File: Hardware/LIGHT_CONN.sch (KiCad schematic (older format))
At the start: 72 parts

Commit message: Added PWM generator, More Shift Regs
Moved GPIO pins on MUSE
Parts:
- added R? (x6): 4.7K, symbol R
- added U?: PCA9685BS, symbol PCA9685BS
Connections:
- net labels added: +3.3V, PWM_SCL, PWM_SDA, ~PWM_OE
- wire segments 168 -> 205
- no-connect marks 0 -> 4
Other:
- note added: "RGB LED Strip PWM Generator"
- moved on the sheet: P?, Q?, R?

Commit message: Syncing changes from 9/20 meeting
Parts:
- removed R? (x6): 4.7K, symbol R
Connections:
- net labels removed: ~PWM_OE
- wire segments 205 -> 183

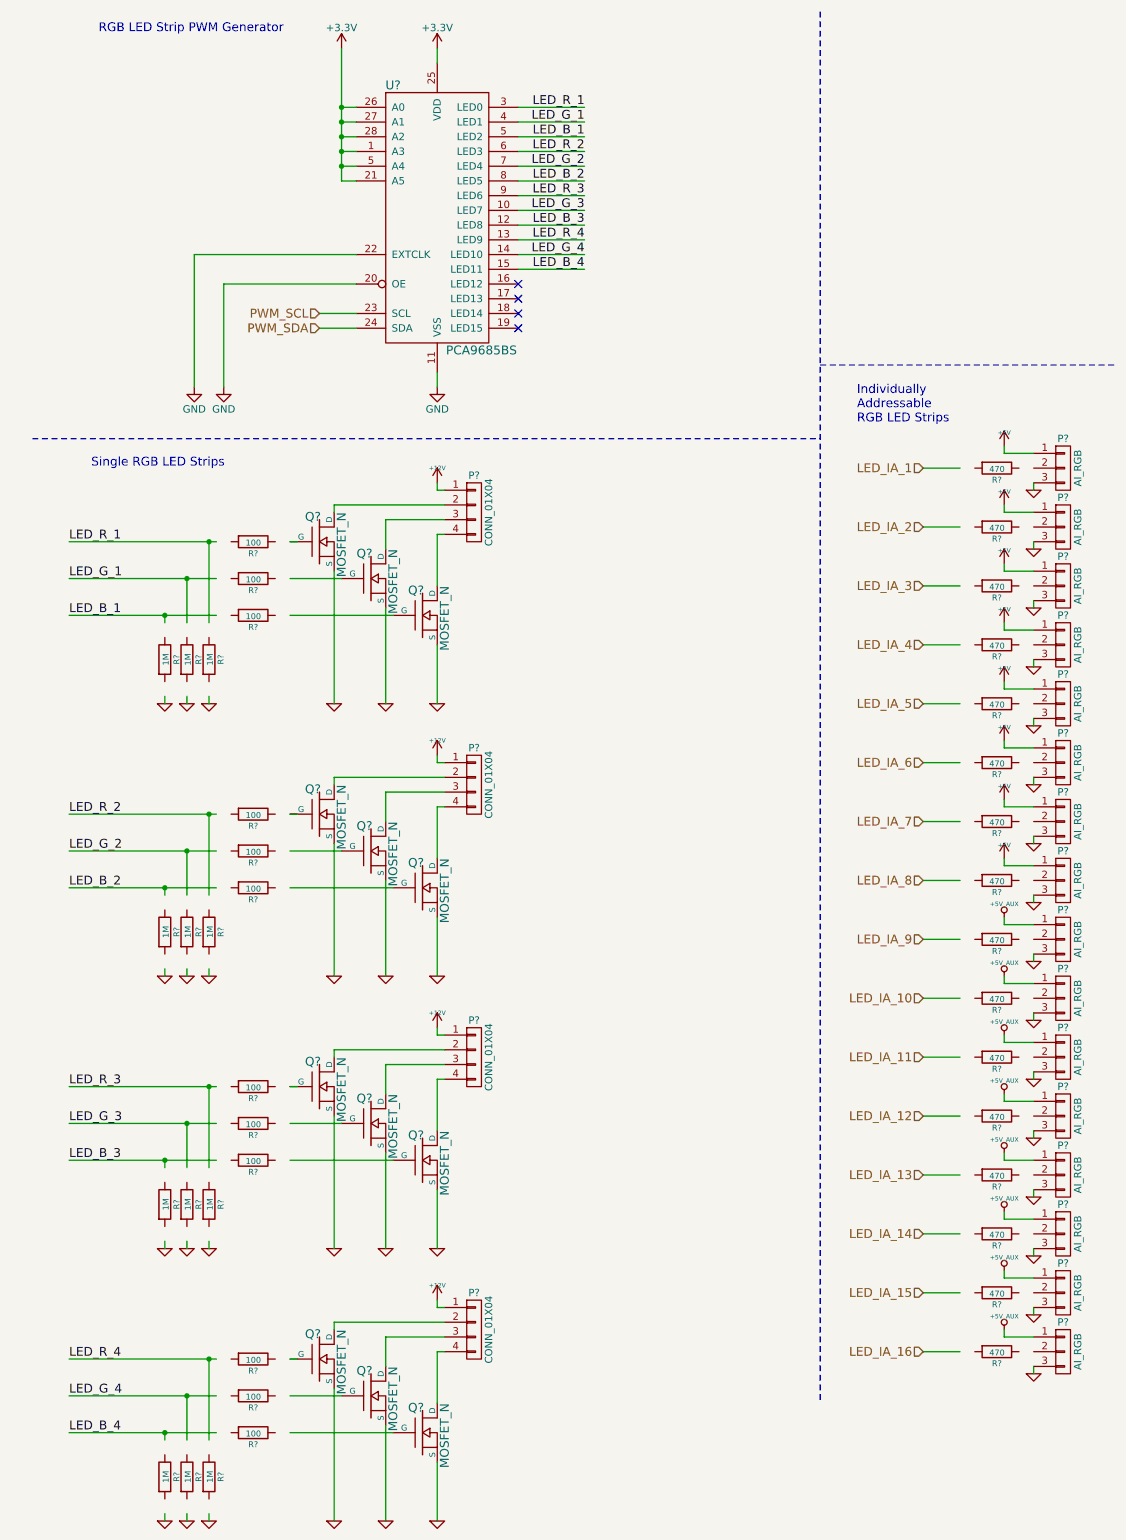
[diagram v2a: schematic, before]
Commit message: Currently adding level shifters
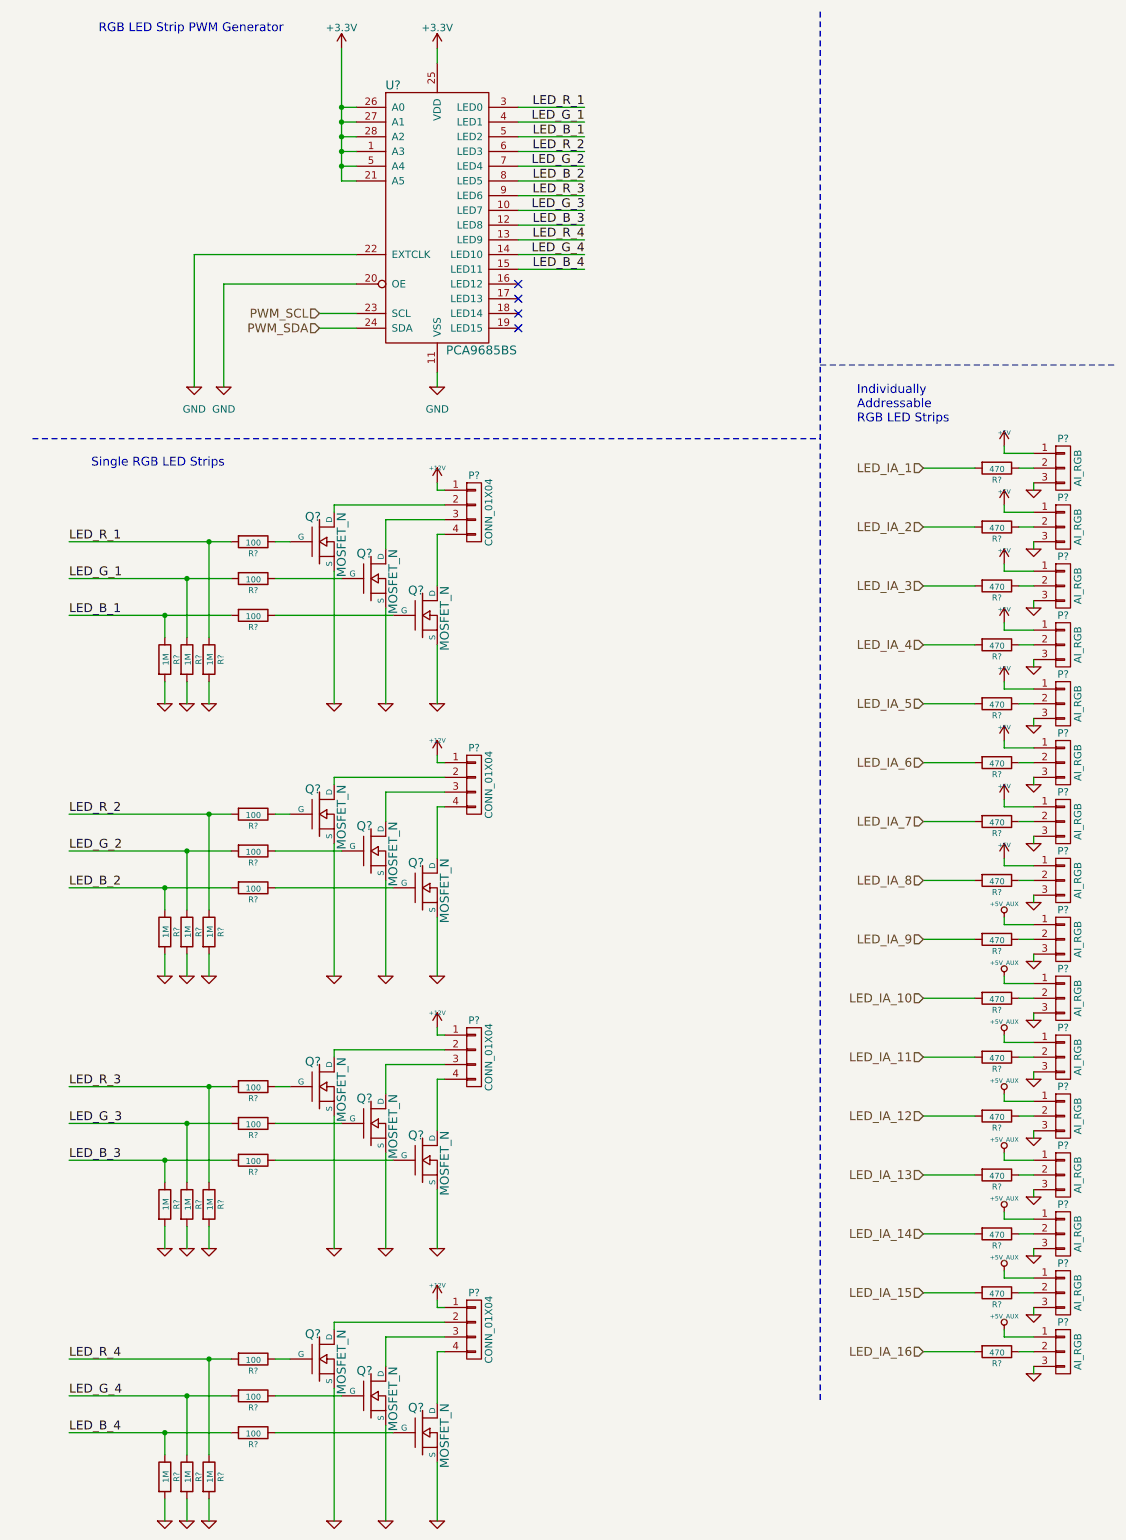
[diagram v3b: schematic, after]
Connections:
- wire segments 183 -> 199
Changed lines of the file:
@@
 LIBS:microchip_pic18mcu
 LIBS:microchip
+LIBS:microchip1
 LIBS:microcontrollers
 LIBS:motorola
@@
 LIBS:sensors
 LIBS:siliconi
+LIBS:special
 LIBS:stm8
 LIBS:stm32
@@
 F 3 "" H 3200 5550 60  0000 C CNN
 	1    3200 5550
-	1    0    0    -1
-$EndComp
-$Comp
-L MOSFET_N Q?
-U 1 1 57E232B5
-P 2400 5950
-F 0 "Q?" H 2410 6120 60  0000 R CNN
-F 1 "MOSFET_N" V 2550 6150 60  0000 R CNN
-F 2 "" H 2400 5950 60  0000 C CNN
-F 3 "" H 2400 5950 60  0000 C CNN
-	1    2400 5950
 	1    0    0    -1
 $EndComp
@@
 $EndComp
 $Comp
-L GND #PWR?
+L GND-RESCUE-museV2 #PWR?
 U 1 1 57E62373
 P 3200 3050
@@
 $EndComp
 $Comp
-L +3.3V #PWR?
+L +3.3V-RESCUE-museV2 #PWR?
 U 1 1 57E6273F
 P 3200 750
+AR Path="/57E6273F" Ref="#PWR?"  Part="1"
+AR Path="/57E226F1/57E6273F" Ref="#PWR?"  Part="1"
 F 0 "#PWR?" H 3200 600 50  0001 C CNN
 F 1 "+3.3V" H 3200 890 50  0000 C CNN
@@
 PWM_SDA
 $Comp
-L GND #PWR?
+L GND-RESCUE-museV2 #PWR?
 U 1 1 57E689F1
 P 1550 3050
@@
 	7250 9750 7250 9700
 Wire Wire Line
-	6500 3600 6750 3600
-Wire Wire Line
-	6750 4000 6500 4000
-Wire Wire Line
-	6750 4400 6500 4400
-Wire Wire Line
-	6750 4800 6500 4800
-Wire Wire Line
-	6750 5200 6500 5200
-Wire Wire Line
-	6750 5600 6500 5600
-Wire Wire Line
-	6750 6000 6500 6000
-Wire Wire Line
-	6500 6400 6750 6400
-Wire Wire Line
-	6750 6800 6500 6800
-Wire Wire Line
-	6500 7200 6750 7200
-Wire Wire Line
-	6750 7600 6500 7600
-Wire Wire Line
-	6500 8000 6750 8000
-Wire Wire Line
-	6750 8400 6500 8400
-Wire Wire Line
-	6500 8800 6750 8800
-Wire Wire Line
-	6750 9200 6500 9200
-Wire Wire Line
-	6500 9600 6750 9600
-Wire Wire Line
-	700  4600 1700 4600
-Wire Wire Line
-	700  4350 1700 4350
-Wire Wire Line
-	700  4100 1700 4100
-Wire Wire Line
-	2200 4100 2250 4100
-Wire Wire Line
-	2200 4350 2550 4350
-Wire Wire Line
-	2200 4600 2900 4600
+	6500 3600 6850 3600
+Wire Wire Line
+	6500 4000 6850 4000
+Wire Wire Line
+	6500 4400 6850 4400
+Wire Wire Line
+	6500 4800 6850 4800
+Wire Wire Line
+	6500 5200 6850 5200
+Wire Wire Line
+	6500 5600 6850 5600
+Wire Wire Line
+	6500 6000 6850 6000
+Wire Wire Line
+	6500 6400 6850 6400
+Wire Wire Line
+	6500 6800 6850 6800
+Wire Wire Line
+	6500 7200 6850 7200
+Wire Wire Line
+	6500 7600 6850 7600
+Wire Wire Line
+	6500 8000 6850 8000
+Wire Wire Line
+	6500 8400 6850 8400
+Wire Wire Line
+	6500 8800 6850 8800
+Wire Wire Line
+	6500 9200 6850 9200
+Wire Wire Line
+	6500 9600 6850 9600
+Wire Wire Line
+	700  4600 1800 4600
+Wire Wire Line
+	700  4350 1800 4350
+Wire Wire Line
+	700  4100 1800 4100
+Wire Wire Line
+	2100 4350 2550 4350
+Wire Wire Line
+	2100 4600 2900 4600
 Wire Wire Line
 	2850 4550 2850 5200
@@
 	2500 4300 2500 5200
 Wire Wire Line
-	1350 4650 1350 4600
+	1350 4600 1350 4750
 Connection ~ 1350 4600
 Wire Wire Line
-	1500 4650 1500 4350
+	1500 4350 1500 4750
 Connection ~ 1500 4350
 Wire Wire Line
-	1650 4650 1650 4100
+	1650 4100 1650 4750
 Connection ~ 1650 4100
 Wire Wire Line
-	1350 5200 1350 5150
-Wire Wire Line
-	1500 5200 1500 5150
-Wire Wire Line
-	1650 5200 1650 5150
+	1350 5050 1350 5200
+Wire Wire Line
+	1500 5050 1500 5200
+Wire Wire Line
+	1650 5050 1650 5200
 Wire Wire Line
 	3200 5550 3200 5600
@@
 	3200 7050 3200 6650
 Wire Wire Line
-	700  6450 1700 6450
-Wire Wire Line
-	700  6200 1700 6200
-Wire Wire Line
-	700  5950 1700 5950
-Wire Wire Line
-	2200 5950 2250 5950
-Wire Wire Line
-	2200 6200 2550 6200
-Wire Wire Line
-	2200 6450 2900 6450
+	700  6450 1800 6450
+Wire Wire Line
+	700  6200 1800 6200
+Wire Wire Line
+	700  5950 1800 5950
+Wire Wire Line
+	2100 6200 2550 6200
+Wire Wire Line
+	2100 6450 2900 6450
 Wire Wire Line
 	2850 6400 2850 7050
@@
 	2500 6150 2500 7050
 Wire Wire Line
-	1350 6500 1350 6450
+	1350 6450 1350 6600
 Connection ~ 1350 6450
 Wire Wire Line
-	1500 6500 1500 6200
+	1500 6200 1500 6600
 Connection ~ 1500 6200
 Wire Wire Line
-	1650 6500 1650 5950
+	1650 5950 1650 6600
 Connection ~ 1650 5950
 Wire Wire Line
-	1350 7050 1350 7000
-Wire Wire Line
-	1500 7050 1500 7000
-Wire Wire Line
-	1650 7050 1650 7000
+	1350 6900 1350 7050
+Wire Wire Line
+	1500 6900 1500 7050
+Wire Wire Line
+	1650 6900 1650 7050
 Wire Wire Line
 	3200 7400 3200 7450
@@
 	3200 8900 3200 8500
 Wire Wire Line
-	700  8300 1700 8300
-Wire Wire Line
-	700  8050 1700 8050
-Wire Wire Line
-	700  7800 1700 7800
-Wire Wire Line
-	2200 7800 2250 7800
-Wire Wire Line
-	2200 8050 2550 8050
-Wire Wire Line
-	2200 8300 2900 8300
+	700  8300 1800 8300
+Wire Wire Line
+	700  8050 1800 8050
+Wire Wire Line
+	700  7800 1800 7800
+Wire Wire Line
+	2100 8050 2550 8050
+Wire Wire Line
+	2100 8300 2900 8300
 Wire Wire Line
 	2850 8250 2850 8900
@@
 	2500 8000 2500 8900
 Wire Wire Line
-	1350 8350 1350 8300
+	1350 8300 1350 8450
 Connection ~ 1350 8300
 Wire Wire Line
-	1500 8350 1500 8050
+	1500 8050 1500 8450
 Connection ~ 1500 8050
 Wire Wire Line
-	1650 8350 1650 7800
+	1650 7800 1650 8450
 Connection ~ 1650 7800
 Wire Wire Line
-	1350 8900 1350 8850
-Wire Wire Line
-	1500 8900 1500 8850
-Wire Wire Line
-	1650 8900 1650 8850
+	1350 8750 1350 8900
+Wire Wire Line
+	1500 8750 1500 8900
+Wire Wire Line
+	1650 8750 1650 8900
 Wire Wire Line
 	3200 9250 3200 9300
@@
 	3200 10750 3200 10350
 Wire Wire Line
-	700  10150 1700 10150
-Wire Wire Line
-	700  9900 1700 9900
-Wire Wire Line
-	700  9650 1700 9650
-Wire Wire Line
-	2200 9650 2250 9650
-Wire Wire Line
-	2200 9900 2550 9900
-Wire Wire Line
-	2200 10150 2900 10150
+	700  10150 1800 10150
+Wire Wire Line
+	700  9900 1800 9900
+Wire Wire Line
+	700  9650 1800 9650
+Wire Wire Line
+	2100 9900 2550 9900
+Wire Wire Line
+	2100 10150 2900 10150
 Wire Wire Line
 	2850 10100 2850 10750
@@
 	2500 9850 2500 10750
 Wire Wire Line
-	1350 10200 1350 10150
+	1350 10150 1350 10300
 Connection ~ 1350 10150
 Wire Wire Line
-	1500 10200 1500 9900
+	1500 9900 1500 10300
 Connection ~ 1500 9900
 Wire Wire Line
-	1650 10200 1650 9650
+	1650 9650 1650 10300
 Connection ~ 1650 9650
 Wire Wire Line
-	1350 10750 1350 10700
-Wire Wire Line
-	1500 10750 1500 10700
-Wire Wire Line
-	1650 10750 1650 10700
+	1350 10600 1350 10750
+Wire Wire Line
+	1500 10600 1500 10750
+Wire Wire Line
+	1650 10600 1650 10750
 Text Notes 900  650  0    60   ~ 0
 RGB LED Strip PWM Generator
 $Comp
-L +3.3V #PWR?
+L +3.3V-RESCUE-museV2 #PWR?
 U 1 1 57EA76FD
 P 2550 750
+AR Path="/57EA76FD" Ref="#PWR?"  Part="1"
+AR Path="/57E226F1/57EA76FD" Ref="#PWR?"  Part="1"
 F 0 "#PWR?" H 2550 600 50  0001 C CNN
 F 1 "+3.3V" H 2550 890 50  0000 C CNN
@@
 Connection ~ 2550 1150
 $Comp
-L GND #PWR?
+L GND-RESCUE-museV2 #PWR?
 U 1 1 57EF1660
 P 1750 3050
@@
 Wire Wire Line
 	1750 2350 2650 2350
+Wire Wire Line
+	2200 9650 2100 9650
+Wire Wire Line
+	2200 7800 2100 7800
+$Comp
+L MOSFET_N Q?
+U 1 1 57E232B5
+P 2400 5950
+F 0 "Q?" H 2410 6120 60  0000 R CNN
+F 1 "MOSFET_N" V 2550 6150 60  0000 R CNN
+F 2 "" H 2400 5950 60  0000 C CNN
+F 3 "" H 2400 5950 60  0000 C CNN
+	1    2400 5950
+	1    0    0    -1
+$EndComp
+Wire Wire Line
+	2200 5950 2100 5950
+Wire Wire Line
+	2200 4100 2100 4100
+Wire Wire Line
+	7150 3600 7250 3600
+Wire Wire Line
+	7150 4000 7250 4000
+Wire Wire Line
+	7250 4400 7150 4400
+Wire Wire Line
+	7150 4800 7250 4800
+Wire Wire Line
+	7250 5200 7150 5200
+Wire Wire Line
+	7150 5600 7250 5600
+Wire Wire Line
+	7250 6000 7150 6000
+Wire Wire Line
+	7150 6400 7250 6400
+Wire Wire Line
+	7250 6800 7150 6800
+Wire Wire Line
+	7150 7200 7250 7200
+Wire Wire Line
+	7250 7600 7150 7600
+Wire Wire Line
+	7150 8000 7250 8000
+Wire Wire Line
+	7250 8400 7150 8400
+Wire Wire Line
+	7250 8800 7150 8800
+Wire Wire Line
+	7150 9200 7250 9200
+Wire Wire Line
+	7250 9600 7150 9600
 $EndSCHEMATC

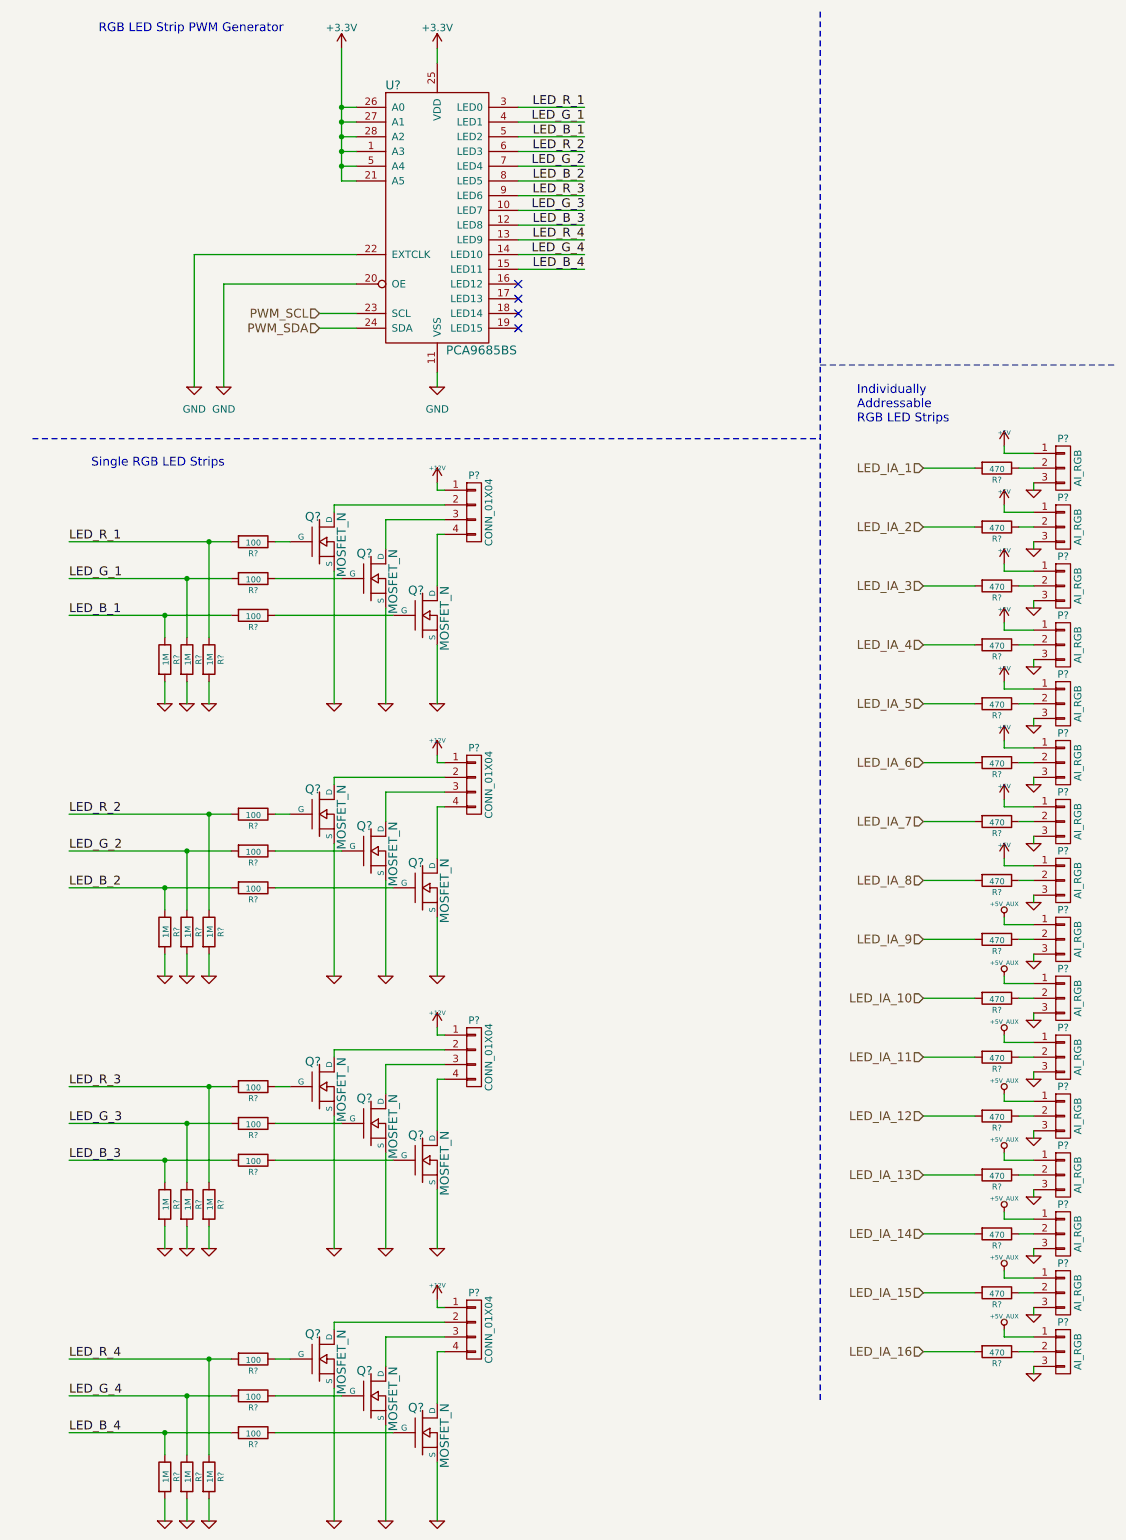
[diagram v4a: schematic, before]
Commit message: Changing to global labels/pages in progress
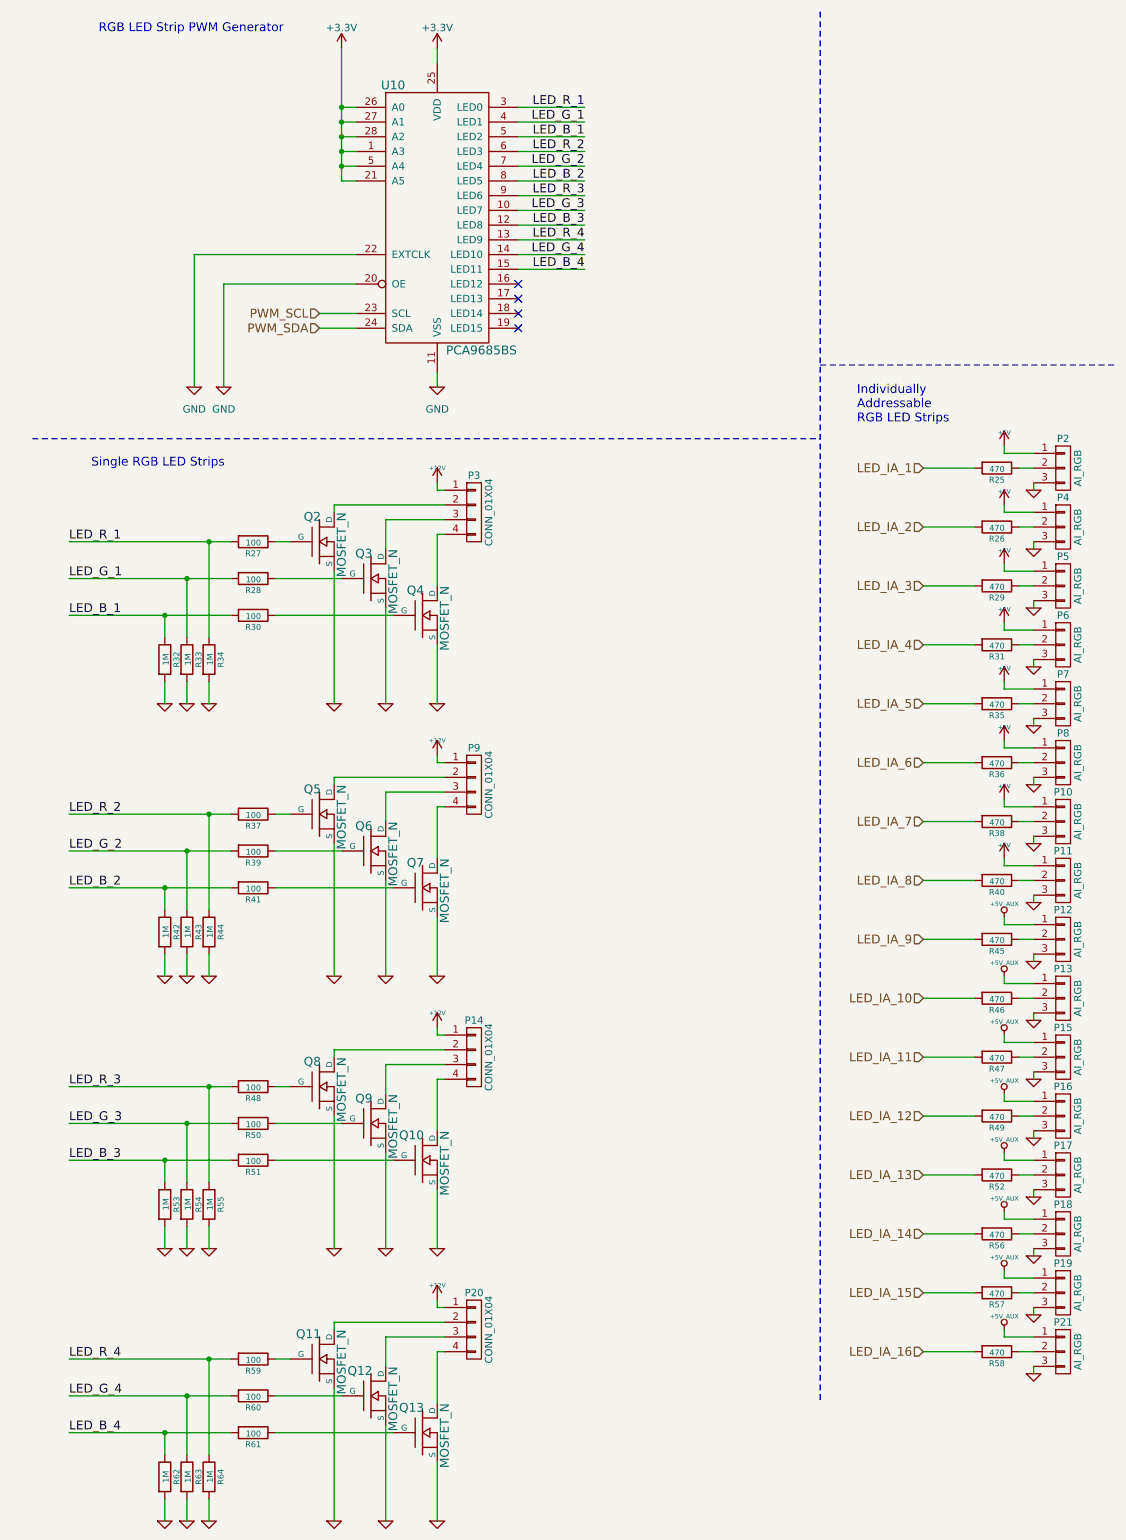
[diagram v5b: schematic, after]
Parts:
- gave numbers to parts that had none: 73
